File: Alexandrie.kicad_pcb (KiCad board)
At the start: 2 copper layers, 100 x 100 mm, 47 parts, among them J1 kk_10, J11 CONN_01X03, J2 kk_5, J3 kk_5, J4 CONN_01X06, J5 CONN_01X02, J6 CONN_01X13, J7 CONN_01X06, J8 kk_10, U1 74HCT04, U12 LD29150DT50R, U2 74HCT04, U3 TPIC6B595, U4 TPIC6B595, U6 TPIC6B595, U7 TPIC6B595

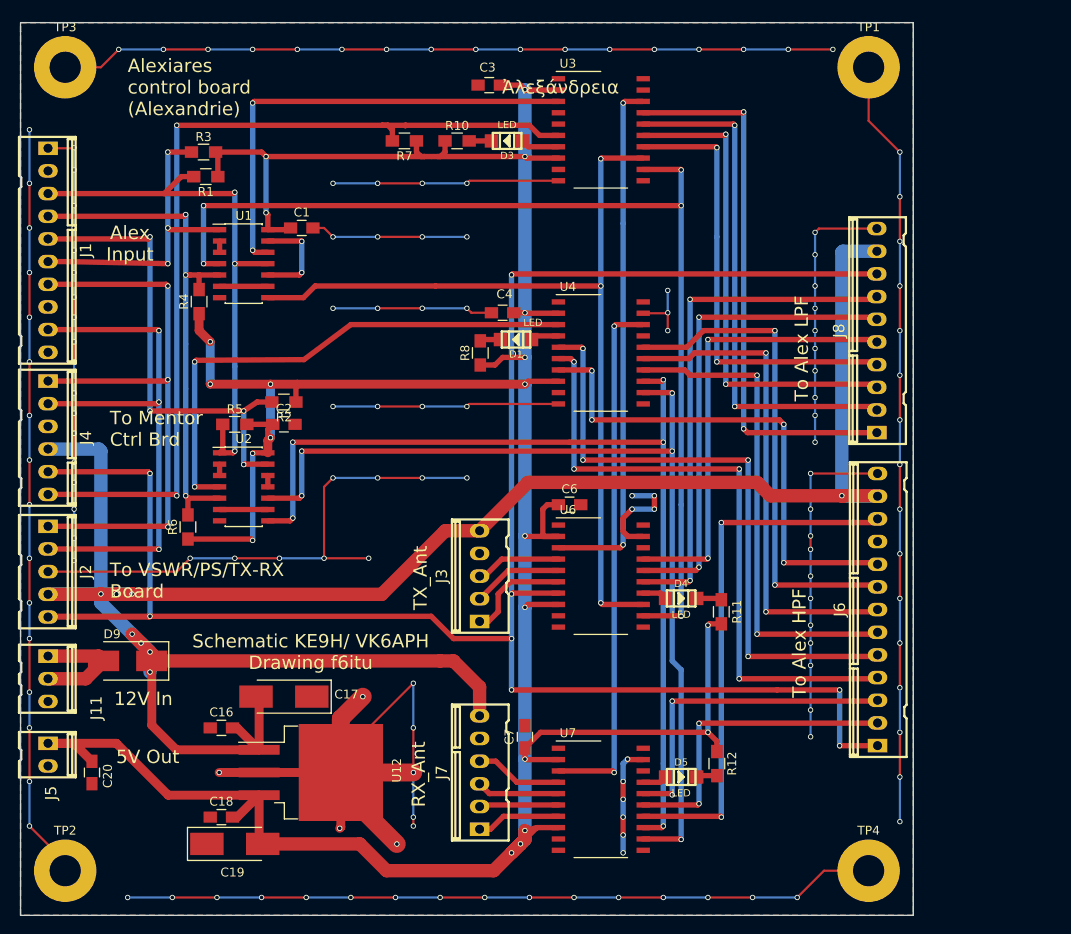
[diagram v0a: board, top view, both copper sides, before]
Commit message: via stitching added, new gerber
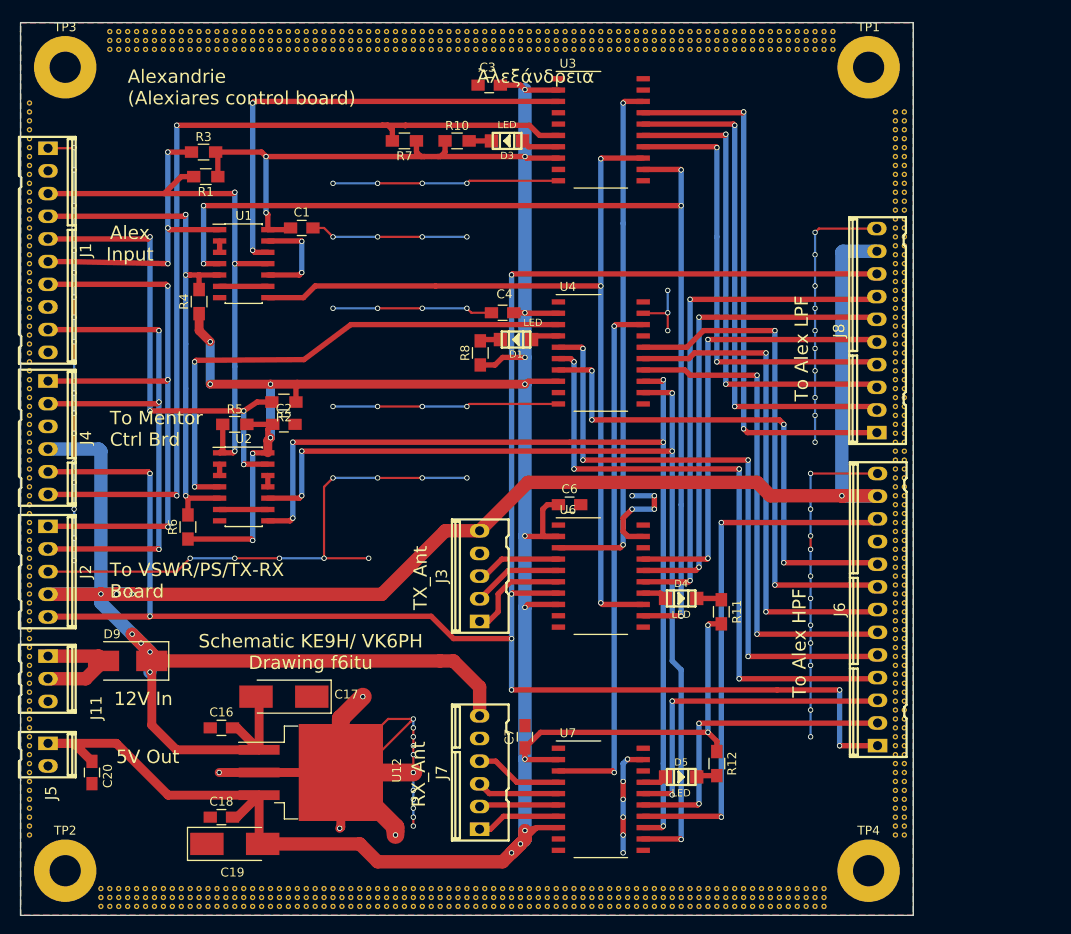
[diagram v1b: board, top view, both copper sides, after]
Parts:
- added REF**: via, via:via, F.Cu at (90.0, 134.0)
- added REF**: via, via:via, F.Cu at (90.0, 125.0)
- added REF**: via, via:via, F.Cu at (163.0, 142.0)
- added REF**: via, via:via, F.Cu at (162.0, 142.0)
- added REF**: via, via:via, F.Cu at (161.0, 142.0)
- added REF**: via, via:via, F.Cu at (160.0, 142.0)
- added REF**: via, via:via, F.Cu at (159.0, 142.0)
- added REF**: via, via:via, F.Cu at (158.0, 142.0)
- added REF**: via, via:via, F.Cu at (157.0, 142.0)
- added REF**: via, via:via, F.Cu at (156.0, 142.0)
- added REF**: via, via:via, F.Cu at (155.0, 142.0)
- added REF**: via, via:via, F.Cu at (154.0, 142.0)
- added REF**: via, via:via, F.Cu at (90.0, 124.0)
- added REF**: via, via:via, F.Cu at (153.0, 142.0)
- added REF**: via, via:via, F.Cu at (152.0, 142.0)
- added REF**: via, via:via, F.Cu at (151.0, 142.0)
- added REF**: via, via:via, F.Cu at (150.0, 142.0)
- added REF**: via, via:via, F.Cu at (149.0, 142.0)
- added REF**: via, via:via, F.Cu at (148.0, 142.0)
- added REF**: via, via:via, F.Cu at (147.0, 142.0)
- added REF**: via, via:via, F.Cu at (146.0, 142.0)
- added REF**: via, via:via, F.Cu at (145.0, 142.0)
- added REF**: via, via:via, F.Cu at (144.0, 142.0)
- added REF**: via, via:via, F.Cu at (90.0, 123.0)
- added REF**: via, via:via, F.Cu at (143.0, 142.0)
- added REF**: via, via:via, F.Cu at (142.0, 142.0)
- added REF**: via, via:via, F.Cu at (141.0, 142.0)
- added REF**: via, via:via, F.Cu at (140.0, 142.0)
- added REF**: via, via:via, F.Cu at (139.0, 142.0)
- added REF**: via, via:via, F.Cu at (138.0, 142.0)
- added REF**: via, via:via, F.Cu at (137.0, 142.0)
- added REF**: via, via:via, F.Cu at (136.0, 142.0)
- added REF**: via, via:via, F.Cu at (135.0, 142.0)
- added REF**: via, via:via, F.Cu at (134.0, 142.0)
- added REF**: via, via:via, F.Cu at (90.0, 122.0)
- added REF**: via, via:via, F.Cu at (133.0, 142.0)
- added REF**: via, via:via, F.Cu at (132.0, 142.0)
- added REF**: via, via:via, F.Cu at (131.0, 142.0)
- added REF**: via, via:via, F.Cu at (130.0, 142.0)
- added REF**: via, via:via, F.Cu at (129.0, 142.0)
- added REF**: via, via:via, F.Cu at (128.0, 142.0)
- added REF**: via, via:via, F.Cu at (127.0, 142.0)
- added REF**: via, via:via, F.Cu at (126.0, 142.0)
- added REF**: via, via:via, F.Cu at (125.0, 142.0)
- added REF**: via, via:via, F.Cu at (124.0, 142.0)
- added REF**: via, via:via, F.Cu at (90.0, 121.0)
- added REF**: via, via:via, F.Cu at (123.0, 142.0)
- added REF**: via, via:via, F.Cu at (122.0, 142.0)
- added REF**: via, via:via, F.Cu at (121.0, 142.0)
- added REF**: via, via:via, F.Cu at (120.0, 142.0)
- added REF**: via, via:via, F.Cu at (119.0, 142.0)
- added REF**: via, via:via, F.Cu at (118.0, 142.0)
- added REF**: via, via:via, F.Cu at (117.0, 142.0)
- added REF**: via, via:via, F.Cu at (116.0, 142.0)
- added REF**: via, via:via, F.Cu at (115.0, 142.0)
- added REF**: via, via:via, F.Cu at (114.0, 142.0)
- added REF**: via, via:via, F.Cu at (90.0, 120.0)
- added REF**: via, via:via, F.Cu at (113.0, 142.0)
- added REF**: via, via:via, F.Cu at (112.0, 142.0)
- added REF**: via, via:via, F.Cu at (111.0, 142.0)
- added REF**: via, via:via, F.Cu at (110.0, 142.0)
- added REF**: via, via:via, F.Cu at (109.0, 142.0)
- added REF**: via, via:via, F.Cu at (108.0, 142.0)
- added REF**: via, via:via, F.Cu at (107.0, 142.0)
- added REF**: via, via:via, F.Cu at (106.0, 142.0)
- added REF**: via, via:via, F.Cu at (105.0, 142.0)
- added REF**: via, via:via, F.Cu at (104.0, 142.0)
- added REF**: via, via:via, F.Cu at (90.0, 119.0)
- added REF**: via, via:via, F.Cu at (103.0, 142.0)
- added REF**: via, via:via, F.Cu at (102.0, 142.0)
- added REF**: via, via:via, F.Cu at (101.0, 142.0)
- added REF**: via, via:via, F.Cu at (100.0, 142.0)
- added REF**: via, via:via, F.Cu at (99.0, 142.0)
- added REF**: via, via:via, F.Cu at (98.0, 142.0)
- added REF**: via, via:via, F.Cu at (179.0, 141.0)
- added REF**: via, via:via, F.Cu at (178.0, 141.0)
- added REF**: via, via:via, F.Cu at (177.0, 141.0)
- added REF**: via, via:via, F.Cu at (176.0, 141.0)
- added REF**: via, via:via, F.Cu at (90.0, 118.0)
- added REF**: via, via:via, F.Cu at (175.0, 141.0)
- added REF**: via, via:via, F.Cu at (174.0, 141.0)
- added REF**: via, via:via, F.Cu at (173.0, 141.0)
- added REF**: via, via:via, F.Cu at (172.0, 141.0)
- added REF**: via, via:via, F.Cu at (171.0, 141.0)
- added REF**: via, via:via, F.Cu at (170.0, 141.0)
- added REF**: via, via:via, F.Cu at (169.0, 141.0)
- added REF**: via, via:via, F.Cu at (168.0, 141.0)
- added REF**: via, via:via, F.Cu at (167.0, 141.0)
- added REF**: via, via:via, F.Cu at (166.0, 141.0)
- added REF**: via, via:via, F.Cu at (90.0, 117.0)
- added REF**: via, via:via, F.Cu at (165.0, 141.0)
- added REF**: via, via:via, F.Cu at (164.0, 141.0)
- added REF**: via, via:via, F.Cu at (163.0, 141.0)
- added REF**: via, via:via, F.Cu at (162.0, 141.0)
- added REF**: via, via:via, F.Cu at (161.0, 141.0)
- added REF**: via, via:via, F.Cu at (160.0, 141.0)
- added REF**: via, via:via, F.Cu at (159.0, 141.0)
- added REF**: via, via:via, F.Cu at (158.0, 141.0)
- added REF**: via, via:via, F.Cu at (157.0, 141.0)
- added REF**: via, via:via, F.Cu at (156.0, 141.0)
- added REF**: via, via:via, F.Cu at (90.0, 116.0)
- added REF**: via, via:via, F.Cu at (155.0, 141.0)
- added REF**: via, via:via, F.Cu at (154.0, 141.0)
- added REF**: via, via:via, F.Cu at (153.0, 141.0)
- added REF**: via, via:via, F.Cu at (152.0, 141.0)
- added REF**: via, via:via, F.Cu at (151.0, 141.0)
- added REF**: via, via:via, F.Cu at (150.0, 141.0)
- added REF**: via, via:via, F.Cu at (149.0, 141.0)
- added REF**: via, via:via, F.Cu at (148.0, 141.0)
- added REF**: via, via:via, F.Cu at (147.0, 141.0)
- added REF**: via, via:via, F.Cu at (146.0, 141.0)
- added REF**: via, via:via, F.Cu at (90.0, 133.0)
- added REF**: via, via:via, F.Cu at (90.0, 115.0)
- added REF**: via, via:via, F.Cu at (145.0, 141.0)
- added REF**: via, via:via, F.Cu at (144.0, 141.0)
- added REF**: via, via:via, F.Cu at (143.0, 141.0)
- added REF**: via, via:via, F.Cu at (142.0, 141.0)
- added REF**: via, via:via, F.Cu at (141.0, 141.0)
- added REF**: via, via:via, F.Cu at (140.0, 141.0)
- added REF**: via, via:via, F.Cu at (139.0, 141.0)
- added REF**: via, via:via, F.Cu at (138.0, 141.0)
- added REF**: via, via:via, F.Cu at (137.0, 141.0)
- added REF**: via, via:via, F.Cu at (136.0, 141.0)
- added REF**: via, via:via, F.Cu at (90.0, 114.0)
- added REF**: via, via:via, F.Cu at (135.0, 141.0)
- added REF**: via, via:via, F.Cu at (134.0, 141.0)
- added REF**: via, via:via, F.Cu at (133.0, 141.0)
- added REF**: via, via:via, F.Cu at (132.0, 141.0)
- added REF**: via, via:via, F.Cu at (131.0, 141.0)
- added REF**: via, via:via, F.Cu at (130.0, 141.0)
- added REF**: via, via:via, F.Cu at (129.0, 141.0)
- added REF**: via, via:via, F.Cu at (128.0, 141.0)
- added REF**: via, via:via, F.Cu at (127.0, 141.0)
- added REF**: via, via:via, F.Cu at (126.0, 141.0)
- added REF**: via, via:via, F.Cu at (90.0, 113.0)
- added REF**: via, via:via, F.Cu at (125.0, 141.0)
- added REF**: via, via:via, F.Cu at (124.0, 141.0)
- added REF**: via, via:via, F.Cu at (123.0, 141.0)
- added REF**: via, via:via, F.Cu at (122.0, 141.0)
- added REF**: via, via:via, F.Cu at (121.0, 141.0)
- added REF**: via, via:via, F.Cu at (120.0, 141.0)
- added REF**: via, via:via, F.Cu at (119.0, 141.0)
- added REF**: via, via:via, F.Cu at (118.0, 141.0)
- added REF**: via, via:via, F.Cu at (117.0, 141.0)
- added REF**: via, via:via, F.Cu at (116.0, 141.0)
- added REF**: via, via:via, F.Cu at (90.0, 112.0)
- added REF**: via, via:via, F.Cu at (115.0, 141.0)
- added REF**: via, via:via, F.Cu at (114.0, 141.0)
- added REF**: via, via:via, F.Cu at (113.0, 141.0)
- added REF**: via, via:via, F.Cu at (112.0, 141.0)
- added REF**: via, via:via, F.Cu at (111.0, 141.0)
- added REF**: via, via:via, F.Cu at (110.0, 141.0)
- added REF**: via, via:via, F.Cu at (109.0, 141.0)
- added REF**: via, via:via, F.Cu at (108.0, 141.0)
- added REF**: via, via:via, F.Cu at (107.0, 141.0)
- added REF**: via, via:via, F.Cu at (106.0, 141.0)
- added REF**: via, via:via, F.Cu at (90.0, 111.0)
- added REF**: via, via:via, F.Cu at (105.0, 141.0)
- added REF**: via, via:via, F.Cu at (104.0, 141.0)
- added REF**: via, via:via, F.Cu at (103.0, 141.0)
- added REF**: via, via:via, F.Cu at (102.0, 141.0)
- added REF**: via, via:via, F.Cu at (101.0, 141.0)
- added REF**: via, via:via, F.Cu at (100.0, 141.0)
- added REF**: via, via:via, F.Cu at (99.0, 141.0)
- added REF**: via, via:via, F.Cu at (98.0, 141.0)
- added REF**: via, via:via, F.Cu at (179.0, 140.0)
- added REF**: via, via:via, F.Cu at (178.0, 140.0)
- added REF**: via, via:via, F.Cu at (90.0, 110.0)
- added REF**: via, via:via, F.Cu at (177.0, 140.0)
- added REF**: via, via:via, F.Cu at (176.0, 140.0)
- added REF**: via, via:via, F.Cu at (175.0, 140.0)
- added REF**: via, via:via, F.Cu at (174.0, 140.0)
- added REF**: via, via:via, F.Cu at (173.0, 140.0)
- added REF**: via, via:via, F.Cu at (172.0, 140.0)
- added REF**: via, via:via, F.Cu at (171.0, 140.0)
- added REF**: via, via:via, F.Cu at (170.0, 140.0)
- added REF**: via, via:via, F.Cu at (169.0, 140.0)
- added REF**: via, via:via, F.Cu at (168.0, 140.0)
- added REF**: via, via:via, F.Cu at (90.0, 109.0)
- added REF**: via, via:via, F.Cu at (167.0, 140.0)
- added REF**: via, via:via, F.Cu at (166.0, 140.0)
- added REF**: via, via:via, F.Cu at (165.0, 140.0)
- added REF**: via, via:via, F.Cu at (164.0, 140.0)
- added REF**: via, via:via, F.Cu at (163.0, 140.0)
- added REF**: via, via:via, F.Cu at (162.0, 140.0)
- added REF**: via, via:via, F.Cu at (161.0, 140.0)
- added REF**: via, via:via, F.Cu at (160.0, 140.0)
- added REF**: via, via:via, F.Cu at (159.0, 140.0)
- added REF**: via, via:via, F.Cu at (158.0, 140.0)
- added REF**: via, via:via, F.Cu at (90.0, 108.0)
- added REF**: via, via:via, F.Cu at (157.0, 140.0)
- added REF**: via, via:via, F.Cu at (156.0, 140.0)
- added REF**: via, via:via, F.Cu at (155.0, 140.0)
- added REF**: via, via:via, F.Cu at (154.0, 140.0)
- added REF**: via, via:via, F.Cu at (153.0, 140.0)
- added REF**: via, via:via, F.Cu at (152.0, 140.0)
- added REF**: via, via:via, F.Cu at (151.0, 140.0)
- added REF**: via, via:via, F.Cu at (150.0, 140.0)
- added REF**: via, via:via, F.Cu at (149.0, 140.0)
- added REF**: via, via:via, F.Cu at (148.0, 140.0)
- added REF**: via, via:via, F.Cu at (90.0, 107.0)
- added REF**: via, via:via, F.Cu at (147.0, 140.0)
- added REF**: via, via:via, F.Cu at (146.0, 140.0)
- added REF**: via, via:via, F.Cu at (145.0, 140.0)
- added REF**: via, via:via, F.Cu at (144.0, 140.0)
- added REF**: via, via:via, F.Cu at (143.0, 140.0)
- added REF**: via, via:via, F.Cu at (142.0, 140.0)
- added REF**: via, via:via, F.Cu at (141.0, 140.0)
- added REF**: via, via:via, F.Cu at (140.0, 140.0)
- added REF**: via, via:via, F.Cu at (139.0, 140.0)
- added REF**: via, via:via, F.Cu at (138.0, 140.0)
- added REF**: via, via:via, F.Cu at (90.0, 106.0)
- added REF**: via, via:via, F.Cu at (137.0, 140.0)
- added REF**: via, via:via, F.Cu at (136.0, 140.0)
- added REF**: via, via:via, F.Cu at (135.0, 140.0)
- added REF**: via, via:via, F.Cu at (134.0, 140.0)
- added REF**: via, via:via, F.Cu at (133.0, 140.0)
- added REF**: via, via:via, F.Cu at (132.0, 140.0)
- added REF**: via, via:via, F.Cu at (131.0, 140.0)
- added REF**: via, via:via, F.Cu at (130.0, 140.0)
- added REF**: via, via:via, F.Cu at (129.0, 140.0)
- added REF**: via, via:via, F.Cu at (128.0, 140.0)
- added REF**: via, via:via, F.Cu at (90.0, 132.0)
- added REF**: via, via:via, F.Cu at (90.0, 105.0)
- added REF**: via, via:via, F.Cu at (127.0, 140.0)
- added REF**: via, via:via, F.Cu at (126.0, 140.0)
- added REF**: via, via:via, F.Cu at (125.0, 140.0)
- added REF**: via, via:via, F.Cu at (124.0, 140.0)
- added REF**: via, via:via, F.Cu at (123.0, 140.0)
- added REF**: via, via:via, F.Cu at (122.0, 140.0)
- added REF**: via, via:via, F.Cu at (121.0, 140.0)
- added REF**: via, via:via, F.Cu at (120.0, 140.0)
- added REF**: via, via:via, F.Cu at (119.0, 140.0)
- added REF**: via, via:via, F.Cu at (118.0, 140.0)
- added REF**: via, via:via, F.Cu at (90.0, 104.0)
- added REF**: via, via:via, F.Cu at (117.0, 140.0)
- added REF**: via, via:via, F.Cu at (116.0, 140.0)
- added REF**: via, via:via, F.Cu at (115.0, 140.0)
- added REF**: via, via:via, F.Cu at (114.0, 140.0)
- added REF**: via, via:via, F.Cu at (113.0, 140.0)
- added REF**: via, via:via, F.Cu at (112.0, 140.0)
- added REF**: via, via:via, F.Cu at (111.0, 140.0)
- added REF**: via, via:via, F.Cu at (110.0, 140.0)
- added REF**: via, via:via, F.Cu at (109.0, 140.0)
- added REF**: via, via:via, F.Cu at (108.0, 140.0)
- added REF**: via, via:via, F.Cu at (90.0, 103.0)
- added REF**: via, via:via, F.Cu at (107.0, 140.0)
- added REF**: via, via:via, F.Cu at (106.0, 140.0)
- added REF**: via, via:via, F.Cu at (105.0, 140.0)
- added REF**: via, via:via, F.Cu at (104.0, 140.0)
- added REF**: via, via:via, F.Cu at (103.0, 140.0)
- added REF**: via, via:via, F.Cu at (102.0, 140.0)
- added REF**: via, via:via, F.Cu at (101.0, 140.0)
- added REF**: via, via:via, F.Cu at (100.0, 140.0)
- added REF**: via, via:via, F.Cu at (99.0, 140.0)
- added REF**: via, via:via, F.Cu at (98.0, 140.0)
- added REF**: via, via:via, F.Cu at (90.0, 102.0)
- added REF**: via, via:via, F.Cu at (188.0, 134.0)
- added REF**: via, via:via, F.Cu at (187.0, 134.0)
- added REF**: via, via:via, F.Cu at (188.0, 133.0)
- added REF**: via, via:via, F.Cu at (187.0, 133.0)
- added REF**: via, via:via, F.Cu at (188.0, 132.0)
- added REF**: via, via:via, F.Cu at (187.0, 132.0)
- added REF**: via, via:via, F.Cu at (188.0, 131.0)
- added REF**: via, via:via, F.Cu at (187.0, 131.0)
- added REF**: via, via:via, F.Cu at (188.0, 130.0)
- added REF**: via, via:via, F.Cu at (187.0, 130.0)
- added REF**: via, via:via, F.Cu at (90.0, 101.0)
- added REF**: via, via:via, F.Cu at (188.0, 129.0)
- added REF**: via, via:via, F.Cu at (187.0, 129.0)
- added REF**: via, via:via, F.Cu at (188.0, 128.0)
- added REF**: via, via:via, F.Cu at (187.0, 128.0)
- added REF**: via, via:via, F.Cu at (188.0, 127.0)
- added REF**: via, via:via, F.Cu at (187.0, 127.0)
- added REF**: via, via:via, F.Cu at (188.0, 126.0)
- added REF**: via, via:via, F.Cu at (187.0, 126.0)
- added REF**: via, via:via, F.Cu at (188.0, 125.0)
- added REF**: via, via:via, F.Cu at (187.0, 125.0)
- added REF**: via, via:via, F.Cu at (90.0, 100.0)
- added REF**: via, via:via, F.Cu at (188.0, 124.0)
- added REF**: via, via:via, F.Cu at (187.0, 124.0)
- added REF**: via, via:via, F.Cu at (188.0, 123.0)
- added REF**: via, via:via, F.Cu at (187.0, 123.0)
- added REF**: via, via:via, F.Cu at (188.0, 122.0)
- added REF**: via, via:via, F.Cu at (187.0, 122.0)
- added REF**: via, via:via, F.Cu at (188.0, 121.0)
- added REF**: via, via:via, F.Cu at (187.0, 121.0)
- added REF**: via, via:via, F.Cu at (188.0, 120.0)
- added REF**: via, via:via, F.Cu at (187.0, 120.0)
- added REF**: via, via:via, F.Cu at (90.0, 99.0)
- added REF**: via, via:via, F.Cu at (188.0, 119.0)
- added REF**: via, via:via, F.Cu at (187.0, 119.0)
- added REF**: via, via:via, F.Cu at (188.0, 118.0)
- added REF**: via, via:via, F.Cu at (187.0, 118.0)
- added REF**: via, via:via, F.Cu at (188.0, 117.0)
- added REF**: via, via:via, F.Cu at (187.0, 117.0)
- added REF**: via, via:via, F.Cu at (188.0, 116.0)
- added REF**: via, via:via, F.Cu at (187.0, 116.0)
- added REF**: via, via:via, F.Cu at (188.0, 115.0)
- added REF**: via, via:via, F.Cu at (187.0, 115.0)
- added REF**: via, via:via, F.Cu at (90.0, 98.0)
- added REF**: via, via:via, F.Cu at (188.0, 114.0)
- added REF**: via, via:via, F.Cu at (187.0, 114.0)
- added REF**: via, via:via, F.Cu at (188.0, 113.0)
- added REF**: via, via:via, F.Cu at (187.0, 113.0)
- added REF**: via, via:via, F.Cu at (188.0, 112.0)
- added REF**: via, via:via, F.Cu at (187.0, 112.0)
- added REF**: via, via:via, F.Cu at (188.0, 111.0)
- added REF**: via, via:via, F.Cu at (187.0, 111.0)
- added REF**: via, via:via, F.Cu at (188.0, 110.0)
- added REF**: via, via:via, F.Cu at (187.0, 110.0)
- added REF**: via, via:via, F.Cu at (90.0, 97.0)
- added REF**: via, via:via, F.Cu at (188.0, 109.0)
- added REF**: via, via:via, F.Cu at (187.0, 109.0)
- added REF**: via, via:via, F.Cu at (188.0, 108.0)
- added REF**: via, via:via, F.Cu at (187.0, 108.0)
- added REF**: via, via:via, F.Cu at (188.0, 107.0)
- added REF**: via, via:via, F.Cu at (187.0, 107.0)
- added REF**: via, via:via, F.Cu at (188.0, 106.0)
- added REF**: via, via:via, F.Cu at (187.0, 106.0)
- added REF**: via, via:via, F.Cu at (188.0, 105.0)
- added REF**: via, via:via, F.Cu at (187.0, 105.0)
- added REF**: via, via:via, F.Cu at (90.0, 96.0)
- added REF**: via, via:via, F.Cu at (188.0, 104.0)
- added REF**: via, via:via, F.Cu at (187.0, 104.0)
- added REF**: via, via:via, F.Cu at (188.0, 103.0)
- added REF**: via, via:via, F.Cu at (187.0, 103.0)
- added REF**: via, via:via, F.Cu at (188.0, 102.0)
- added REF**: via, via:via, F.Cu at (187.0, 102.0)
- added REF**: via, via:via, F.Cu at (188.0, 101.0)
- added REF**: via, via:via, F.Cu at (187.0, 101.0)
- added REF**: via, via:via, F.Cu at (188.0, 100.0)
- added REF**: via, via:via, F.Cu at (187.0, 100.0)
- added REF**: via, via:via, F.Cu at (90.0, 131.0)
- added REF**: via, via:via, F.Cu at (90.0, 95.0)
- added REF**: via, via:via, F.Cu at (188.0, 99.0)
- added REF**: via, via:via, F.Cu at (187.0, 99.0)
- added REF**: via, via:via, F.Cu at (188.0, 98.0)
- added REF**: via, via:via, F.Cu at (187.0, 98.0)
- added REF**: via, via:via, F.Cu at (188.0, 97.0)
- added REF**: via, via:via, F.Cu at (187.0, 97.0)
- added REF**: via, via:via, F.Cu at (188.0, 96.0)
- added REF**: via, via:via, F.Cu at (187.0, 96.0)
- added REF**: via, via:via, F.Cu at (188.0, 95.0)
- added REF**: via, via:via, F.Cu at (187.0, 95.0)
- added REF**: via, via:via, F.Cu at (90.0, 94.0)
- added REF**: via, via:via, F.Cu at (188.0, 94.0)
- added REF**: via, via:via, F.Cu at (187.0, 94.0)
- added REF**: via, via:via, F.Cu at (188.0, 93.0)
- added REF**: via, via:via, F.Cu at (187.0, 93.0)
- added REF**: via, via:via, F.Cu at (188.0, 92.0)
- added REF**: via, via:via, F.Cu at (187.0, 92.0)
- added REF**: via, via:via, F.Cu at (188.0, 91.0)
- added REF**: via, via:via, F.Cu at (187.0, 91.0)
- added REF**: via, via:via, F.Cu at (188.0, 90.0)
- added REF**: via, via:via, F.Cu at (187.0, 90.0)
- added REF**: via, via:via, F.Cu at (90.0, 93.0)
- added REF**: via, via:via, F.Cu at (188.0, 89.0)
- added REF**: via, via:via, F.Cu at (187.0, 89.0)
- added REF**: via, via:via, F.Cu at (188.0, 88.0)
- added REF**: via, via:via, F.Cu at (187.0, 88.0)
- added REF**: via, via:via, F.Cu at (188.0, 87.0)
- added REF**: via, via:via, F.Cu at (187.0, 87.0)
- added REF**: via, via:via, F.Cu at (188.0, 86.0)
- added REF**: via, via:via, F.Cu at (187.0, 86.0)
- added REF**: via, via:via, F.Cu at (188.0, 85.0)
- added REF**: via, via:via, F.Cu at (187.0, 85.0)
- added REF**: via, via:via, F.Cu at (90.0, 92.0)
- added REF**: via, via:via, F.Cu at (188.0, 84.0)
- added REF**: via, via:via, F.Cu at (187.0, 84.0)
- added REF**: via, via:via, F.Cu at (188.0, 83.0)
- added REF**: via, via:via, F.Cu at (187.0, 83.0)
- added REF**: via, via:via, F.Cu at (188.0, 82.0)
- added REF**: via, via:via, F.Cu at (187.0, 82.0)
- added REF**: via, via:via, F.Cu at (188.0, 81.0)
- added REF**: via, via:via, F.Cu at (187.0, 81.0)
- added REF**: via, via:via, F.Cu at (188.0, 80.0)
- added REF**: via, via:via, F.Cu at (187.0, 80.0)
- added REF**: via, via:via, F.Cu at (90.0, 91.0)
- added REF**: via, via:via, F.Cu at (188.0, 79.0)
- added REF**: via, via:via, F.Cu at (187.0, 79.0)
- added REF**: via, via:via, F.Cu at (188.0, 78.0)
- added REF**: via, via:via, F.Cu at (187.0, 78.0)
- added REF**: via, via:via, F.Cu at (188.0, 77.0)
- added REF**: via, via:via, F.Cu at (187.0, 77.0)
- added REF**: via, via:via, F.Cu at (188.0, 76.0)
- added REF**: via, via:via, F.Cu at (187.0, 76.0)
- added REF**: via, via:via, F.Cu at (188.0, 75.0)
- added REF**: via, via:via, F.Cu at (187.0, 75.0)
- added REF**: via, via:via, F.Cu at (90.0, 90.0)
- added REF**: via, via:via, F.Cu at (188.0, 74.0)
- added REF**: via, via:via, F.Cu at (187.0, 74.0)
- added REF**: via, via:via, F.Cu at (188.0, 73.0)
- added REF**: via, via:via, F.Cu at (187.0, 73.0)
- added REF**: via, via:via, F.Cu at (188.0, 72.0)
- added REF**: via, via:via, F.Cu at (187.0, 72.0)
- added REF**: via, via:via, F.Cu at (188.0, 71.0)
- added REF**: via, via:via, F.Cu at (187.0, 71.0)
- added REF**: via, via:via, F.Cu at (188.0, 70.0)
- added REF**: via, via:via, F.Cu at (187.0, 70.0)
- added REF**: via, via:via, F.Cu at (90.0, 89.0)
- added REF**: via, via:via, F.Cu at (188.0, 69.0)
- added REF**: via, via:via, F.Cu at (187.0, 69.0)
- added REF**: via, via:via, F.Cu at (188.0, 68.0)
- added REF**: via, via:via, F.Cu at (187.0, 68.0)
- added REF**: via, via:via, F.Cu at (188.0, 67.0)
- added REF**: via, via:via, F.Cu at (187.0, 67.0)
- added REF**: via, via:via, F.Cu at (188.0, 66.0)
- added REF**: via, via:via, F.Cu at (187.0, 66.0)
- added REF**: via, via:via, F.Cu at (188.0, 65.0)
- added REF**: via, via:via, F.Cu at (187.0, 65.0)
- added REF**: via, via:via, F.Cu at (90.0, 88.0)
- added REF**: via, via:via, F.Cu at (188.0, 64.0)
- added REF**: via, via:via, F.Cu at (187.0, 64.0)
- added REF**: via, via:via, F.Cu at (188.0, 63.0)
- added REF**: via, via:via, F.Cu at (187.0, 63.0)
- added REF**: via, via:via, F.Cu at (188.0, 62.0)
- added REF**: via, via:via, F.Cu at (187.0, 62.0)
- added REF**: via, via:via, F.Cu at (188.0, 61.0)
- added REF**: via, via:via, F.Cu at (187.0, 61.0)
- added REF**: via, via:via, F.Cu at (188.0, 60.0)
- added REF**: via, via:via, F.Cu at (187.0, 60.0)
- added REF**: via, via:via, F.Cu at (90.0, 87.0)
- added REF**: via, via:via, F.Cu at (188.0, 59.0)
- added REF**: via, via:via, F.Cu at (187.0, 59.0)
- added REF**: via, via:via, F.Cu at (188.0, 58.0)
- added REF**: via, via:via, F.Cu at (187.0, 58.0)
- added REF**: via, via:via, F.Cu at (188.0, 57.0)
- added REF**: via, via:via, F.Cu at (187.0, 57.0)
- added REF**: via, via:via, F.Cu at (188.0, 56.0)
- added REF**: via, via:via, F.Cu at (187.0, 56.0)
- added REF**: via, via:via, F.Cu at (188.0, 55.0)
- added REF**: via, via:via, F.Cu at (187.0, 55.0)
- added REF**: via, via:via, F.Cu at (90.0, 86.0)
- added REF**: via, via:via, F.Cu at (188.0, 54.0)
- added REF**: via, via:via, F.Cu at (187.0, 54.0)
- added REF**: via, via:via, F.Cu at (188.0, 53.0)
- added REF**: via, via:via, F.Cu at (187.0, 53.0)
- added REF**: via, via:via, F.Cu at (180.0, 46.0)
- added REF**: via, via:via, F.Cu at (179.0, 46.0)
- added REF**: via, via:via, F.Cu at (178.0, 46.0)
- added REF**: via, via:via, F.Cu at (177.0, 46.0)
- added REF**: via, via:via, F.Cu at (176.0, 46.0)
- added REF**: via, via:via, F.Cu at (175.0, 46.0)
- added REF**: via, via:via, F.Cu at (90.0, 130.0)
- added REF**: via, via:via, F.Cu at (90.0, 85.0)
- added REF**: via, via:via, F.Cu at (174.0, 46.0)
- added REF**: via, via:via, F.Cu at (173.0, 46.0)
- added REF**: via, via:via, F.Cu at (172.0, 46.0)
- added REF**: via, via:via, F.Cu at (171.0, 46.0)
- added REF**: via, via:via, F.Cu at (170.0, 46.0)
- added REF**: via, via:via, F.Cu at (169.0, 46.0)
- added REF**: via, via:via, F.Cu at (168.0, 46.0)
- added REF**: via, via:via, F.Cu at (167.0, 46.0)
- added REF**: via, via:via, F.Cu at (166.0, 46.0)
- added REF**: via, via:via, F.Cu at (165.0, 46.0)
- added REF**: via, via:via, F.Cu at (90.0, 84.0)
- added REF**: via, via:via, F.Cu at (164.0, 46.0)
- added REF**: via, via:via, F.Cu at (163.0, 46.0)
- added REF**: via, via:via, F.Cu at (162.0, 46.0)
- added REF**: via, via:via, F.Cu at (161.0, 46.0)
- added REF**: via, via:via, F.Cu at (160.0, 46.0)
- added REF**: via, via:via, F.Cu at (159.0, 46.0)
- added REF**: via, via:via, F.Cu at (158.0, 46.0)
- added REF**: via, via:via, F.Cu at (157.0, 46.0)
- added REF**: via, via:via, F.Cu at (156.0, 46.0)
- added REF**: via, via:via, F.Cu at (155.0, 46.0)
- added REF**: via, via:via, F.Cu at (90.0, 83.0)
- added REF**: via, via:via, F.Cu at (154.0, 46.0)
- added REF**: via, via:via, F.Cu at (153.0, 46.0)
- added REF**: via, via:via, F.Cu at (152.0, 46.0)
- added REF**: via, via:via, F.Cu at (151.0, 46.0)
- added REF**: via, via:via, F.Cu at (150.0, 46.0)
- added REF**: via, via:via, F.Cu at (149.0, 46.0)
- added REF**: via, via:via, F.Cu at (148.0, 46.0)
- added REF**: via, via:via, F.Cu at (147.0, 46.0)
- added REF**: via, via:via, F.Cu at (146.0, 46.0)
- added REF**: via, via:via, F.Cu at (145.0, 46.0)
- added REF**: via, via:via, F.Cu at (90.0, 82.0)
- added REF**: via, via:via, F.Cu at (144.0, 46.0)
- added REF**: via, via:via, F.Cu at (143.0, 46.0)
- added REF**: via, via:via, F.Cu at (142.0, 46.0)
- added REF**: via, via:via, F.Cu at (141.0, 46.0)
- added REF**: via, via:via, F.Cu at (140.0, 46.0)
- added REF**: via, via:via, F.Cu at (139.0, 46.0)
- added REF**: via, via:via, F.Cu at (138.0, 46.0)
- added REF**: via, via:via, F.Cu at (137.0, 46.0)
- added REF**: via, via:via, F.Cu at (136.0, 46.0)
- added REF**: via, via:via, F.Cu at (135.0, 46.0)
- added REF**: via, via:via, F.Cu at (90.0, 81.0)
- added REF**: via, via:via, F.Cu at (134.0, 46.0)
- added REF**: via, via:via, F.Cu at (133.0, 46.0)
- added REF**: via, via:via, F.Cu at (132.0, 46.0)
- added REF**: via, via:via, F.Cu at (131.0, 46.0)
- added REF**: via, via:via, F.Cu at (130.0, 46.0)
- added REF**: via, via:via, F.Cu at (129.0, 46.0)
- added REF**: via, via:via, F.Cu at (128.0, 46.0)
- added REF**: via, via:via, F.Cu at (127.0, 46.0)
- added REF**: via, via:via, F.Cu at (126.0, 46.0)
- added REF**: via, via:via, F.Cu at (125.0, 46.0)
- added REF**: via, via:via, F.Cu at (90.0, 80.0)
- added REF**: via, via:via, F.Cu at (124.0, 46.0)
- added REF**: via, via:via, F.Cu at (123.0, 46.0)
- added REF**: via, via:via, F.Cu at (122.0, 46.0)
- added REF**: via, via:via, F.Cu at (121.0, 46.0)
- added REF**: via, via:via, F.Cu at (120.0, 46.0)
- added REF**: via, via:via, F.Cu at (119.0, 46.0)
- added REF**: via, via:via, F.Cu at (118.0, 46.0)
- added REF**: via, via:via, F.Cu at (117.0, 46.0)
- added REF**: via, via:via, F.Cu at (116.0, 46.0)
- added REF**: via, via:via, F.Cu at (115.0, 46.0)
- added REF**: via, via:via, F.Cu at (90.0, 79.0)
- added REF**: via, via:via, F.Cu at (114.0, 46.0)
- added REF**: via, via:via, F.Cu at (113.0, 46.0)
- added REF**: via, via:via, F.Cu at (112.0, 46.0)
- added REF**: via, via:via, F.Cu at (111.0, 46.0)
- added REF**: via, via:via, F.Cu at (110.0, 46.0)
- added REF**: via, via:via, F.Cu at (109.0, 46.0)
- added REF**: via, via:via, F.Cu at (108.0, 46.0)
- added REF**: via, via:via, F.Cu at (107.0, 46.0)
- added REF**: via, via:via, F.Cu at (106.0, 46.0)
- added REF**: via, via:via, F.Cu at (105.0, 46.0)
- added REF**: via, via:via, F.Cu at (90.0, 78.0)
- added REF**: via, via:via, F.Cu at (104.0, 46.0)
- added REF**: via, via:via, F.Cu at (103.0, 46.0)
- added REF**: via, via:via, F.Cu at (102.0, 46.0)
- added REF**: via, via:via, F.Cu at (101.0, 46.0)
- added REF**: via, via:via, F.Cu at (100.0, 46.0)
- added REF**: via, via:via, F.Cu at (99.0, 46.0)
- added REF**: via, via:via, F.Cu at (180.0, 45.0)
- added REF**: via, via:via, F.Cu at (179.0, 45.0)
- added REF**: via, via:via, F.Cu at (178.0, 45.0)
- added REF**: via, via:via, F.Cu at (177.0, 45.0)
- added REF**: via, via:via, F.Cu at (90.0, 77.0)
- added REF**: via, via:via, F.Cu at (176.0, 45.0)
- added REF**: via, via:via, F.Cu at (175.0, 45.0)
- added REF**: via, via:via, F.Cu at (174.0, 45.0)
- added REF**: via, via:via, F.Cu at (173.0, 45.0)
- added REF**: via, via:via, F.Cu at (172.0, 45.0)
- added REF**: via, via:via, F.Cu at (171.0, 45.0)
- added REF**: via, via:via, F.Cu at (170.0, 45.0)
- added REF**: via, via:via, F.Cu at (169.0, 45.0)
- added REF**: via, via:via, F.Cu at (168.0, 45.0)
- added REF**: via, via:via, F.Cu at (167.0, 45.0)
- added REF**: via, via:via, F.Cu at (90.0, 76.0)
- added REF**: via, via:via, F.Cu at (166.0, 45.0)
- added REF**: via, via:via, F.Cu at (165.0, 45.0)
- added REF**: via, via:via, F.Cu at (164.0, 45.0)
- added REF**: via, via:via, F.Cu at (163.0, 45.0)
- added REF**: via, via:via, F.Cu at (162.0, 45.0)
- added REF**: via, via:via, F.Cu at (161.0, 45.0)
- added REF**: via, via:via, F.Cu at (160.0, 45.0)
- added REF**: via, via:via, F.Cu at (159.0, 45.0)
- added REF**: via, via:via, F.Cu at (158.0, 45.0)
- added REF**: via, via:via, F.Cu at (157.0, 45.0)
- added REF**: via, via:via, F.Cu at (90.0, 129.0)
- added REF**: via, via:via, F.Cu at (90.0, 75.0)
- added REF**: via, via:via, F.Cu at (156.0, 45.0)
- added REF**: via, via:via, F.Cu at (155.0, 45.0)
- added REF**: via, via:via, F.Cu at (154.0, 45.0)
- added REF**: via, via:via, F.Cu at (153.0, 45.0)
- added REF**: via, via:via, F.Cu at (152.0, 45.0)
- added REF**: via, via:via, F.Cu at (151.0, 45.0)
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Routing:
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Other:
- board text added: "Alexandrie Ἀλεξάνδρεια (Alexiares control board)"
- board text added: "Schematic KE9H/ VK6PH Drawing f6itu"
- board text removed: "Alexiares control board Ἀλεξάνδρεια (Alexandrie)"
- board text removed: "Schematic KE9H/ VK6APH Drawing f6itu"

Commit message: silk cleaning
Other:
- board text added: "Gnd +12V TX_RX_RLY 6m 12/10m 17/15m 6m 30/20m 40m 80m 160m"
- board text removed: "Gnd +12V Gnd 6m 12/10m 17/15m 6m 30/20m 40m 80m 160m"
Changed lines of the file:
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@@
     (links 901)
     (no_connects 0)
-    (area 88.924999 42.924999 189.075001 143.075001)
+    (area 86.0088 42.025 191.21726 144.075)
     (thickness 1.6)
     (drawings 27)
@@
     (effects (font (size 1.5 1.5) (thickness 0.3)) (justify left mirror))
   )
-  (gr_text "Gnd\n+12V\nGnd\n6m\n12/10m\n17/15m\n6m 30/20m\n40m\n80m\n160m\n" (at 183.25 77.5) (layer B.SilkS)
+  (gr_text "Gnd\n+12V\nTX_RX_RLY\n6m\n12/10m\n17/15m\n6m 30/20m\n40m\n80m\n160m\n" (at 183.25 77.5) (layer B.SilkS)
     (effects (font (size 1.5 1.5) (thickness 0.3)) (justify left mirror))
   )

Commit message: new gerber, minor mods
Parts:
- J7: value CONN_01X06 -> Conn_01x07; footprint conn_kk100:kk100_22-23-2061 -> Connectors_Molex:Molex_KK-6410-07_07x2.54mm_Straight
- U12: value LD29150DT50R -> 78M05 Dpak
- moved J7 8.75 mm to (140.5, 135.8)
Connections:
- J7 pad 1: RX_BYPASS_OUT -> TX_RX_RLY
- J7 pad 2: RX3_IN -> RX_BYPASS_OUT
- J7 pad 3: RX2_IN -> RX3_IN
- J7 pad 4: Xvtr_IN -> RX2_IN
- J7 pad 5: GND -> Xvtr_IN
- J7 pad 6: +12V -> GND
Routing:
- net GND: track 379.8 -> 425.7 mm, vias 92 -> 214
- net TX_RX_RLY: track 232.2 -> 252.8 mm
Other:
- board text added: "+12V Gnd Xvtr_IN RX2_IN RX3_IN RX_ByPass_OUT TX_RX_RLY"
- board text removed: "+12V Gnd Xvtr_IN RX2_IN RX3_IN RX_ByPass_OUT"

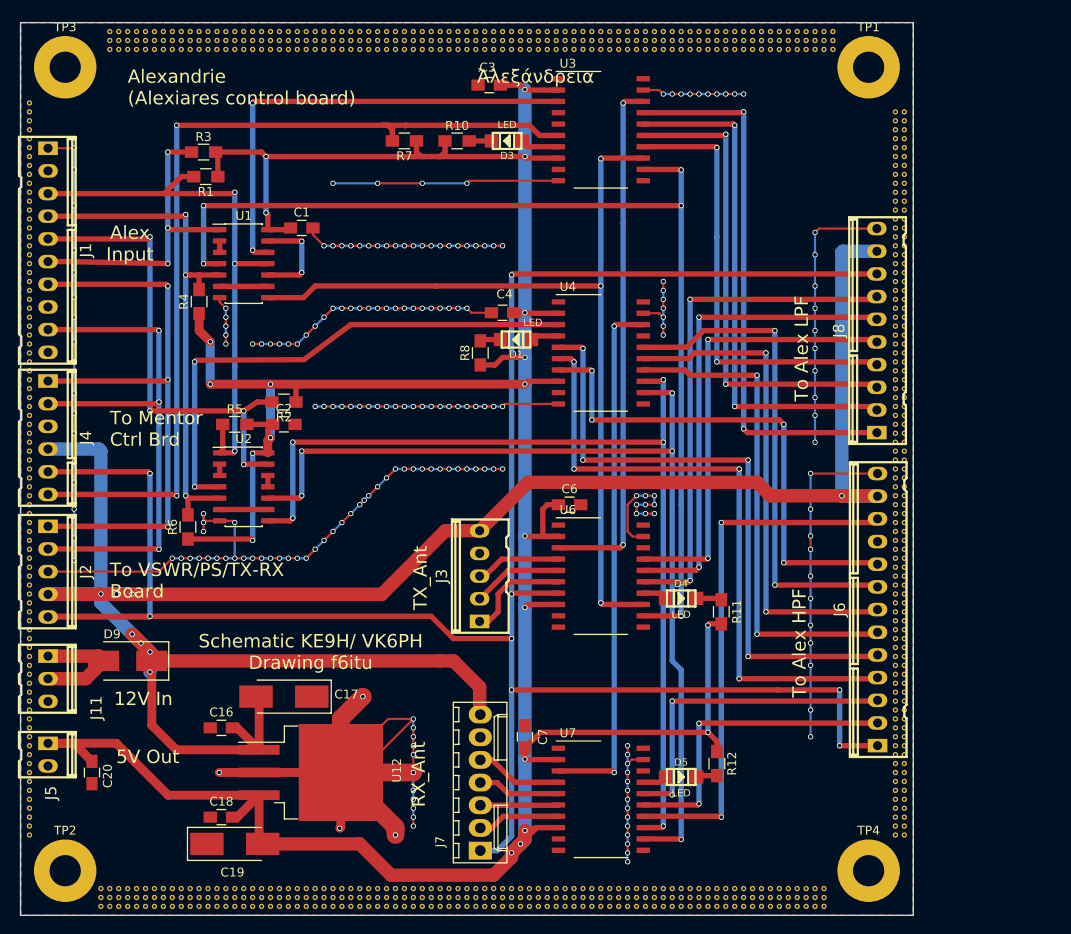
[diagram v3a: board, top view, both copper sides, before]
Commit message: hasl border added
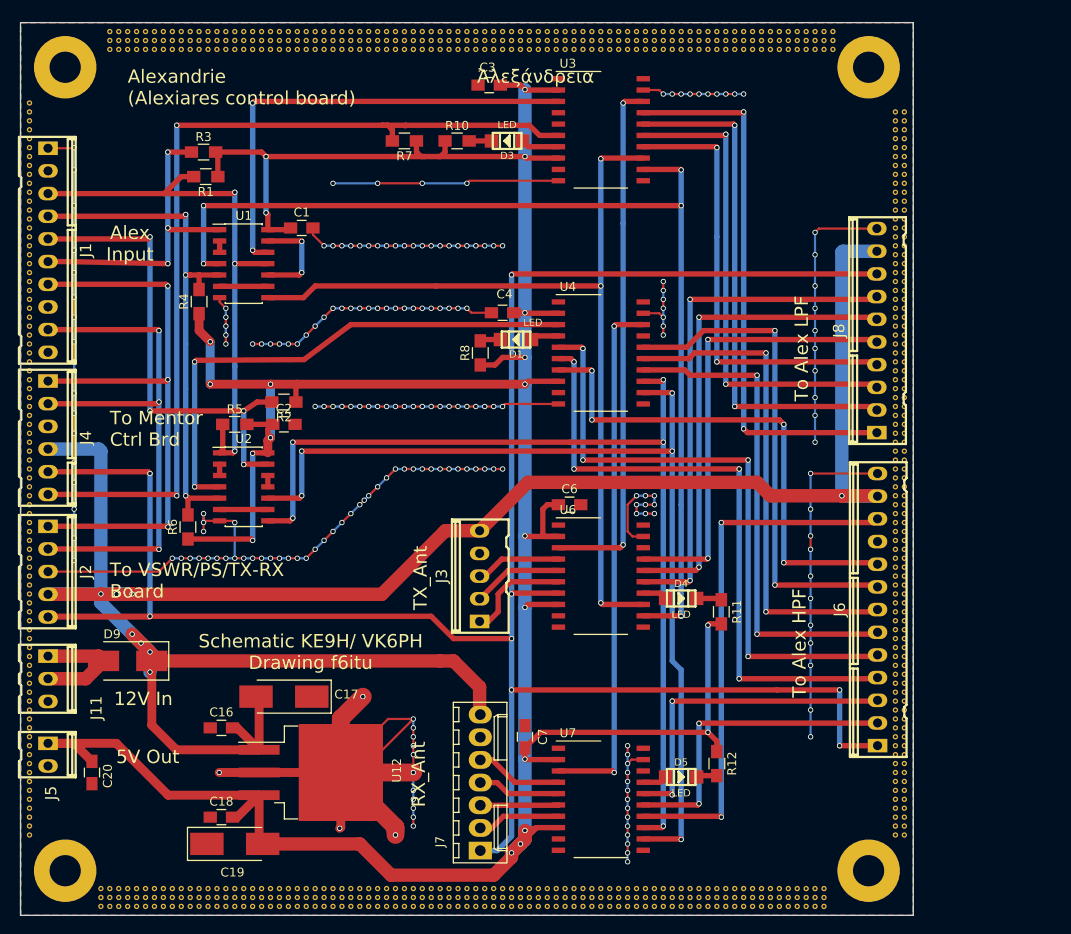
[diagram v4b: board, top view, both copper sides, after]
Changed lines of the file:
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@@
     (descr "Mounting Hole 3.5mm")
     (tags "mounting hole 3.5mm")
-    (fp_text reference TP1 (at 0 -4.5) (layer F.SilkS)
+    (fp_text reference TP1 (at 0 -4.5) (layer F.SilkS) hide
       (effects (font (size 1 1) (thickness 0.15)))
     )
@@
     (descr "Mounting Hole 3.5mm")
     (tags "mounting hole 3.5mm")
-    (fp_text reference TP2 (at 0 -4.5) (layer F.SilkS)
+    (fp_text reference TP2 (at 0 -4.5) (layer F.SilkS) hide
       (effects (font (size 1 1) (thickness 0.15)))
     )
@@
     (descr "Mounting Hole 3.5mm")
     (tags "mounting hole 3.5mm")
-    (fp_text reference TP3 (at 0 -4.5) (layer F.SilkS)
+    (fp_text reference TP3 (at 0 -4.5) (layer F.SilkS) hide
       (effects (font (size 1 1) (thickness 0.15)))
     )
@@
     (descr "Mounting Hole 3.5mm")
     (tags "mounting hole 3.5mm")
-    (fp_text reference TP4 (at 0 -4.5) (layer F.SilkS)
-      (effects (font (size 1 1) (thickness 0.15)))
-    )
-    (fp_text value TEST (at 0 4.5) (layer F.Fab)
+    (fp_text reference TP4 (at 0 -4.5) (layer F.SilkS) hide
+      (effects (font (size 1 1) (thickness 0.15)))
+    )
+    (fp_text value TEST (at 0 4.5) (layer F.Fab) hide
       (effects (font (size 1 1) (thickness 0.15)))
     )
@@
       )
     )
+  )
+  (zone (net 0) (net_name "") (layer F.Mask) (hatch edge 0.508)
+    (connect_pads (clearance 0.508))
+    (min_thickness 0.254)
+    (fill yes (arc_segments 16) (thermal_gap 0.508) (thermal_bridge_width 0.508))
+    (polygon
+      (pts
+        (xy 189 45) (xy 89 45) (xy 89 43) (xy 189 43)
+      )
+    )
+  )
+  (zone (net 0) (net_name "") (layer F.Mask) (hatch edge 0.508)
+    (connect_pads (clearance 0.508))
+    (min_thickness 0.254)
+    (fill yes (arc_segments 16) (thermal_gap 0.508) (thermal_bridge_width 0.508))
+    (polygon
+      (pts
+        (xy 189 143) (xy 89 143) (xy 89 141) (xy 189 141)
+      )
+    )
+  )
+  (zone (net 0) (net_name "") (layer B.Mask) (hatch edge 0.508)
+    (connect_pads (clearance 0.508))
+    (min_thickness 0.254)
+    (fill yes (arc_segments 16) (thermal_gap 0.508) (thermal_bridge_width 0.508))
+    (polygon
+      (pts
+        (xy 189 143) (xy 89 143) (xy 89 141) (xy 189 141)
+      )
+    )
+  )
+  (zone (net 0) (net_name "") (layer B.Mask) (hatch edge 0.508)
+    (connect_pads (clearance 0.508))
+    (min_thickness 0.254)
+    (fill yes (arc_segments 16) (thermal_gap 0.508) (thermal_bridge_width 0.508))
+    (polygon
+      (pts
+        (xy 189 45) (xy 89 45) (xy 89 43) (xy 189 43)
+      )
+    )
